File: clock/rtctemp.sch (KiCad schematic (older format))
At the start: 15 parts, among them U601 ADT7410, U602 DS3231, U603 ADT7410

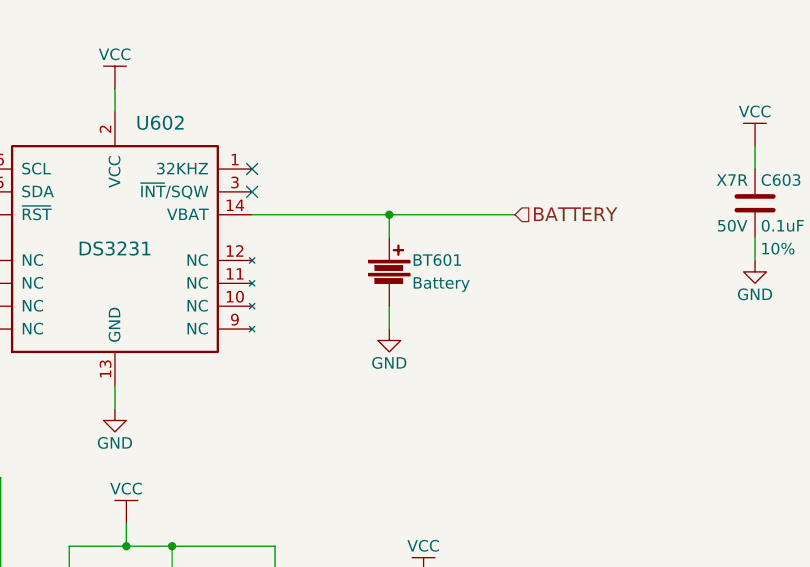
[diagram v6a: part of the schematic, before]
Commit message: Clean up most of the schematic DRC errors. Update placement.
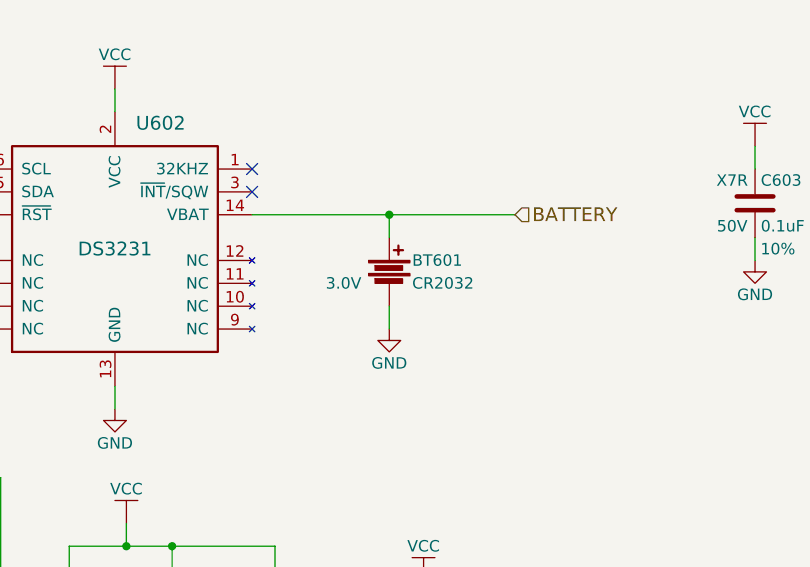
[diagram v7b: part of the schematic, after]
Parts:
- BT601: value Battery -> CR2032; footprint (none) -> local:Battery_Holder_2032_BK-5058; Manufacturer (none) -> Memory Protection Devices; PartNum (none) -> BK-5058; Voltage (none) -> 3.0V
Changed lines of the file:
@@
 RTC_SDA
 $Comp
-L GND #PWR076
+L GND #PWR080
 U 1 1 5636B600
 P 1450 1900
-F 0 "#PWR076" H 1450 1650 50  0001 C CNN
+F 0 "#PWR080" H 1450 1650 50  0001 C CNN
 F 1 "GND" H 1450 1750 50  0000 C CNN
 F 2 "" H 1450 1900 60  0000 C CNN
@@
 	5750 3400 5750 3300
 $Comp
-L GND #PWR077
+L GND #PWR081
 U 1 1 5636B6C4
 P 5750 3400
-F 0 "#PWR077" H 5750 3150 50  0001 C CNN
+F 0 "#PWR081" H 5750 3150 50  0001 C CNN
 F 1 "GND" H 5750 3250 50  0000 C CNN
 F 2 "" H 5750 3400 60  0000 C CNN
@@
 $EndComp
 $Comp
-L VCC #PWR078
+L VCC #PWR082
 U 1 1 5636B791
 P 1450 1300
-F 0 "#PWR078" H 1450 1150 50  0001 C CNN
+F 0 "#PWR082" H 1450 1150 50  0001 C CNN
 F 1 "VCC" H 1450 1450 50  0000 C CNN
 F 2 "" H 1450 1300 60  0000 C CNN
@@
 	1450 1400 1450 1300
 $Comp
-L VCC #PWR079
+L VCC #PWR083
 U 1 1 5636B7D2
 P 5750 2000
-F 0 "#PWR079" H 5750 1850 50  0001 C CNN
+F 0 "#PWR083" H 5750 1850 50  0001 C CNN
 F 1 "VCC" H 5750 2150 50  0000 C CNN
 F 2 "" H 5750 2000 60  0000 C CNN
@@
 	4500 1800 4500 1900
 $Comp
-L VCC #PWR080
+L VCC #PWR084
 U 1 1 5636BBAE
 P 4300 1700
-F 0 "#PWR080" H 4300 1550 50  0001 C CNN
+F 0 "#PWR084" H 4300 1550 50  0001 C CNN
 F 1 "VCC" H 4300 1850 50  0000 C CNN
 F 2 "" H 4300 1700 60  0000 C CNN
@@
 P 6950 2800
 F 0 "BT601" H 7050 2850 50  0000 L CNN
-F 1 "Battery" H 7050 2750 50  0000 L CNN
-F 2 "" V 6950 2840 60  0001 C CNN
+F 1 "CR2032" H 7050 2750 50  0000 L CNN
+F 2 "local:Battery_Holder_2032_BK-5058" V 6950 2840 60  0001 C CNN
 F 3 "" V 6950 2840 60  0000 C CNN
+F 4 "3.0V" H 6750 2750 50  0000 C CNN "Voltage"
+F 5 "Memory Protection Devices" H 6950 2800 60  0001 C CNN "Manufacturer"
+F 6 "BK-5058" H 6950 2800 60  0001 C CNN "PartNum"
 	1    6950 2800
 	1    0    0    -1
@@
 	6950 2550 6950 2650
 $Comp
-L GND #PWR081
+L GND #PWR085
 U 1 1 5636BC94
 P 6950 3050
-F 0 "#PWR081" H 6950 2800 50  0001 C CNN
+F 0 "#PWR085" H 6950 2800 50  0001 C CNN
 F 1 "GND" H 6950 2900 50  0000 C CNN
 F 2 "" H 6950 3050 60  0000 C CNN
@@
 $EndComp
 $Comp
-L VCC #PWR082
+L VCC #PWR086
 U 1 1 5636C0D5
 P 4200 4150
-F 0 "#PWR082" H 4200 4000 50  0001 C CNN
+F 0 "#PWR086" H 4200 4000 50  0001 C CNN
 F 1 "VCC" H 4200 4300 50  0000 C CNN
 F 2 "" H 4200 4150 60  0000 C CNN
@@
 	7100 5350 7100 5250
 $Comp
-L GND #PWR083
+L GND #PWR087
 U 1 1 5636C104
 P 7100 5350
-F 0 "#PWR083" H 7100 5100 50  0001 C CNN
+F 0 "#PWR087" H 7100 5100 50  0001 C CNN
 F 1 "GND" H 7100 5200 50  0000 C CNN
 F 2 "" H 7100 5350 60  0000 C CNN
@@
 	4200 5350 4200 5250
 $Comp
-L GND #PWR084
+L GND #PWR088
 U 1 1 5636C11B
 P 4200 5350
-F 0 "#PWR084" H 4200 5100 50  0001 C CNN
+F 0 "#PWR088" H 4200 5100 50  0001 C CNN
 F 1 "GND" H 4200 5200 50  0000 C CNN
 F 2 "" H 4200 5350 60  0000 C CNN
@@
 	6000 4000 6000 4100
 $Comp
-L VCC #PWR085
+L VCC #PWR089
 U 1 1 5636C1AA
 P 5800 3900
-F 0 "#PWR085" H 5800 3750 50  0001 C CNN
+F 0 "#PWR089" H 5800 3750 50  0001 C CNN
 F 1 "VCC" H 5800 4050 50  0000 C CNN
 F 2 "" H 5800 3900 60  0000 C CNN
@@
 Connection ~ 3550 5550
 $Comp
-L GND #PWR086
+L GND #PWR090
 U 1 1 5636C550
 P 3550 5650
-F 0 "#PWR086" H 3550 5400 50  0001 C CNN
+F 0 "#PWR090" H 3550 5400 50  0001 C CNN
 F 1 "GND" H 3550 5500 50  0000 C CNN
 F 2 "" H 3550 5650 60  0000 C CNN
@@
 	6450 4950 6450 5150
 $Comp
-L GND #PWR087
+L GND #PWR091
 U 1 1 5636C5CD
 P 6450 5550
-F 0 "#PWR087" H 6450 5300 50  0001 C CNN
+F 0 "#PWR091" H 6450 5300 50  0001 C CNN
 F 1 "GND" H 6450 5400 50  0000 C CNN
 F 2 "" H 6450 5550 60  0000 C CNN
@@
 Connection ~ 3500 4650
 $Comp
-L GND #PWR088
+L GND #PWR092
 U 1 1 5636CF30
 P 8550 2750
-F 0 "#PWR088" H 8550 2500 50  0001 C CNN
+F 0 "#PWR092" H 8550 2500 50  0001 C CNN
 F 1 "GND" H 8550 2600 50  0000 C CNN
 F 2 "" H 8550 2750 60  0000 C CNN
@@
 $EndComp
 $Comp
-L VCC #PWR089
+L VCC #PWR093
 U 1 1 5636D2DE
 P 8550 2250
-F 0 "#PWR089" H 8550 2100 50  0001 C CNN
+F 0 "#PWR093" H 8550 2100 50  0001 C CNN
 F 1 "VCC" H 8550 2400 50  0000 C CNN
 F 2 "" H 8550 2250 60  0000 C CNN
@@
 $EndComp
 $Comp
-L GND #PWR090
+L GND #PWR094
 U 1 1 5636D43C
 P 4150 6600
-F 0 "#PWR090" H 4150 6350 50  0001 C CNN
+F 0 "#PWR094" H 4150 6350 50  0001 C CNN
 F 1 "GND" H 4150 6450 50  0000 C CNN
 F 2 "" H 4150 6600 60  0000 C CNN
@@
 $EndComp
 $Comp
-L VCC #PWR091
+L VCC #PWR095
 U 1 1 5636D44F
 P 4150 6100
-F 0 "#PWR091" H 4150 5950 50  0001 C CNN
+F 0 "#PWR095" H 4150 5950 50  0001 C CNN
 F 1 "VCC" H 4150 6250 50  0000 C CNN
 F 2 "" H 4150 6100 60  0000 C CNN
@@
 $EndComp
 $Comp
-L GND #PWR092
+L GND #PWR096
 U 1 1 5636D49F
 P 6150 6600
-F 0 "#PWR092" H 6150 6350 50  0001 C CNN
+F 0 "#PWR096" H 6150 6350 50  0001 C CNN
 F 1 "GND" H 6150 6450 50  0000 C CNN
 F 2 "" H 6150 6600 60  0000 C CNN
@@
 $EndComp
 $Comp
-L VCC #PWR093
+L VCC #PWR097
 U 1 1 5636D4B2
 P 6150 6100
-F 0 "#PWR093" H 6150 5950 50  0001 C CNN
+F 0 "#PWR097" H 6150 5950 50  0001 C CNN
 F 1 "VCC" H 6150 6250 50  0000 C CNN
 F 2 "" H 6150 6100 60  0000 C CNN
@@
 NoConn ~ 6350 2350
 $Comp
-L VCC #PWR094
+L VCC #PWR098
 U 1 1 563E1DA8
 P 7100 4150
-F 0 "#PWR094" H 7100 4000 50  0001 C CNN
+F 0 "#PWR098" H 7100 4000 50  0001 C CNN
 F 1 "VCC" H 7100 4300 50  0000 C CNN
 F 2 "" H 7100 4150 60  0000 C CNN

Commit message: Checkpoint PCB placement.
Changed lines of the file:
@@
 Wire Wire Line
 	6450 5550 6450 5450
+$Comp
+L PWR_FLAG #FLG099
+U 1 1 564556C2
+P 7250 2450
+F 0 "#FLG099" H 7250 2545 50  0001 C CNN
+F 1 "PWR_FLAG" H 7250 2630 50  0000 C CNN
+F 2 "" H 7250 2450 60  0000 C CNN
+F 3 "" H 7250 2450 60  0000 C CNN
+	1    7250 2450
+	1    0    0    -1
+$EndComp
+Wire Wire Line
+	7250 2450 7250 2550
+Connection ~ 7250 2550
 $EndSCHEMATC
